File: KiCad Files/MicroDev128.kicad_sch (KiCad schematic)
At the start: 24 parts, among them J1 UPDI Header, J3 GPIO, J4 PWR and ANALOG, SW1 SW_SP3T, SW2 RST, U1 AVR128DB32x-xRXB, U2 LT8653SEV_PBF

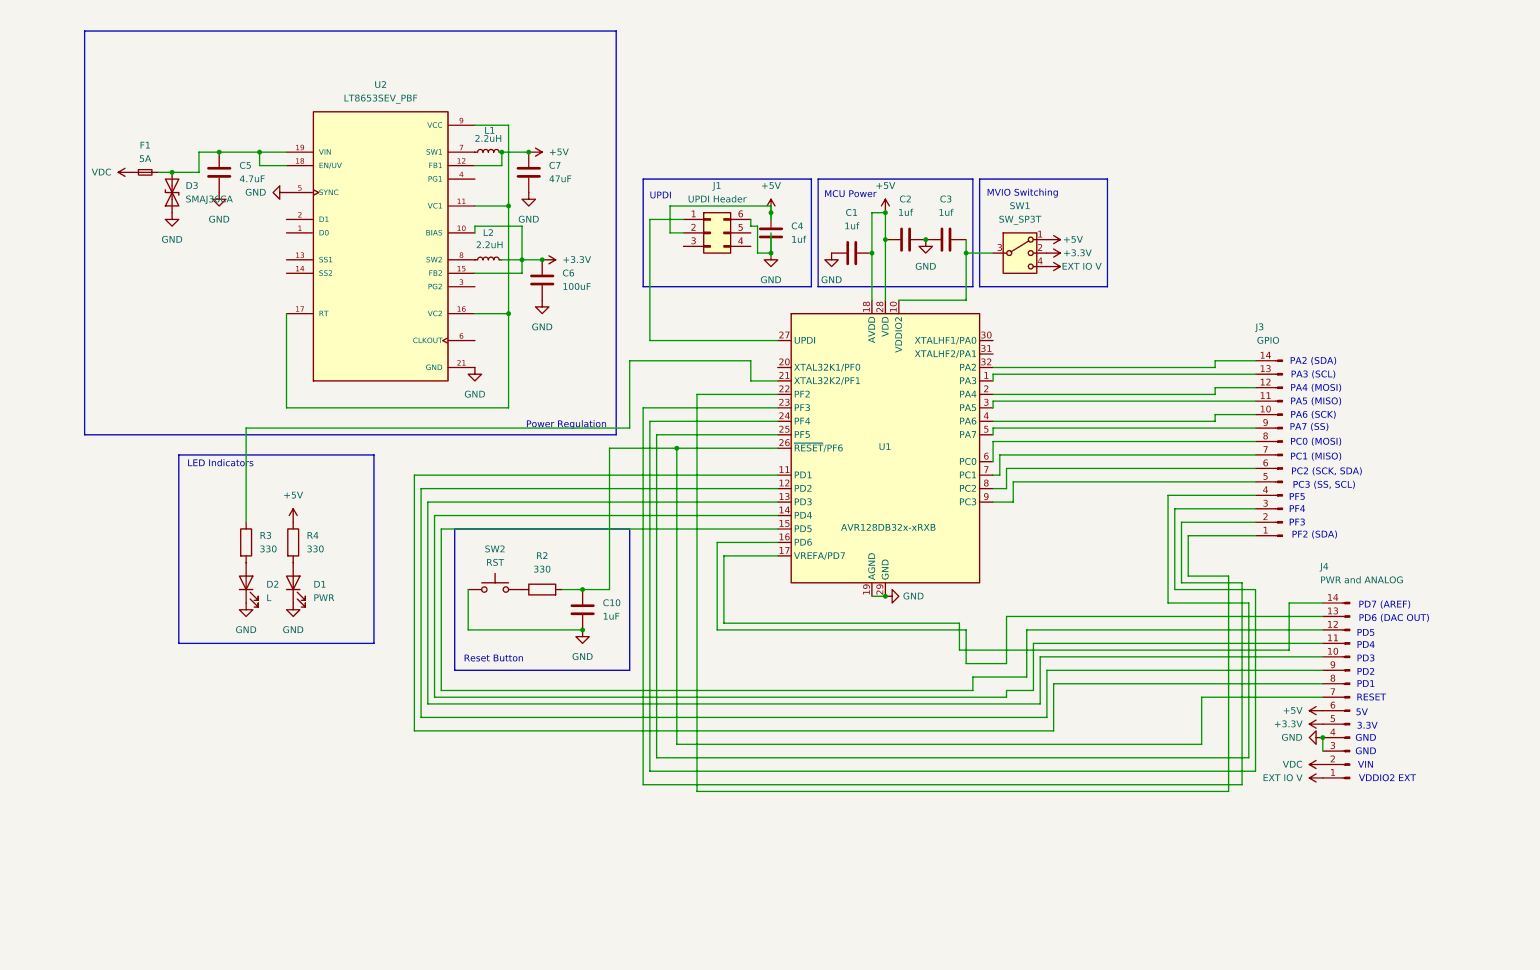
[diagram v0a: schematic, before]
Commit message: Updated PCB, fixed errors, and added more docs
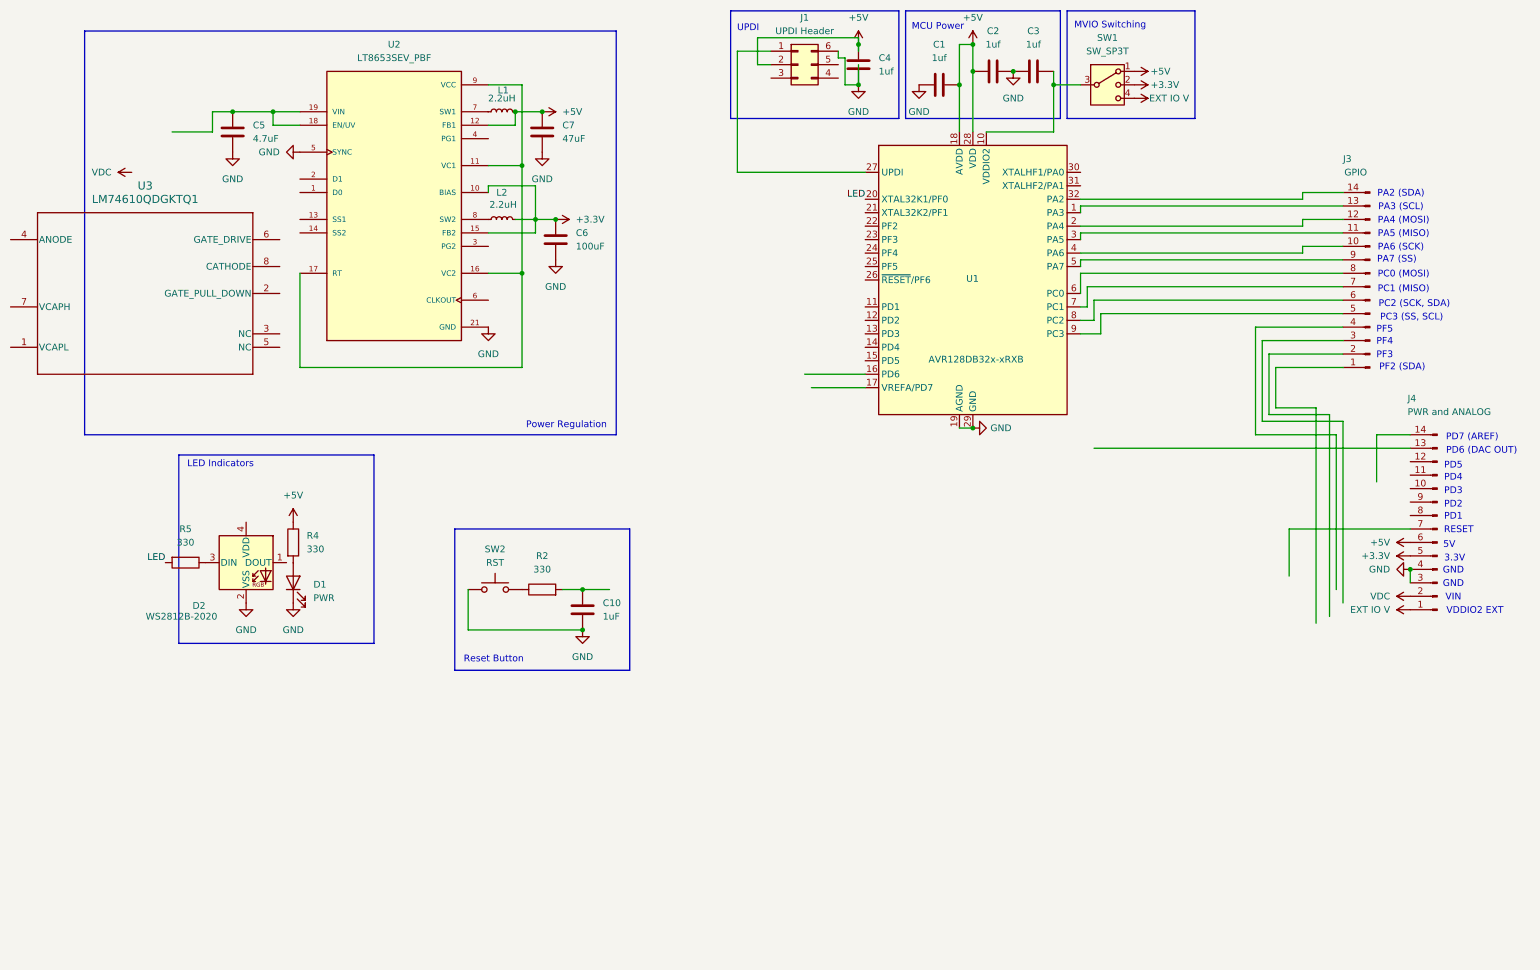
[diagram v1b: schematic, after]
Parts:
- removed D2: L, LED_SMD:LED_0603_1608Metric, symbol Device:LED
- removed D3: SMAJ36CA, Diode_SMD:D_SMA, symbol Device:D_TVS
- removed F1: 5A, Fuse:Fuse_0603_1608Metric, symbol Device:Fuse_Small
- removed R3: 330, Resistor_SMD:R_0402_1005Metric, symbol Device:R
- added D2: WS2812B-2020, LED_SMD:LED_WS2812B-2020_PLCC4_2.0x2.0mm, symbol LED:WS2812B-2020
- added R5: 330, Resistor_SMD:R_0402_1005Metric, symbol Device:R
- added U3: LM74610QDGKTQ1, DGK0008A_N, symbol LM7610:LM74610QDGKTQ1
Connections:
- net GND: now also D2.2 (VSS)
- net at U1.11 (PD1): no longer J4.8 (Pin_8)
- net at U1.12 (PD2): no longer J4.9 (Pin_9)
- net at U1.13 (PD3): no longer J4.10 (Pin_10)
- net at U1.14 (PD4): no longer J4.11 (Pin_11)
- net at U1.15 (PD5): no longer J4.12 (Pin_12)
- net at U1.16 (PD6): no longer J4.13 (Pin_13)
- net at U1.17 (VREFA/PD7): no longer J4.14 (Pin_14)
- net LED: now reaches U1.20 (XTAL32K1/PF0)
- net LED: now also R5.2
- net at U1.22 (PF2): no longer J3.1 (Pin_1)
- net at U1.23 (PF3): no longer J3.2 (Pin_2)
- net at U1.24 (PF4): no longer J3.3 (Pin_3)
- net at U1.25 (PF5): no longer J3.4 (Pin_4)
- net at C10.1, R2.2: no longer J4.7 (Pin_7), U1.26 (~{RESET}/PF6)
- new net: D2.3 (DIN), R5.1
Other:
- moved on the sheet: C1, C2, C3, C4, C5, C6, C7, J1, J3, J4, L1, L2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

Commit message: Started on Rev1B
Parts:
- added C8: 2.2uF, Capacitor_SMD:C_0402_1005Metric, symbol Device:C
- added C9: 100nF, symbol Device:C_Small
- added F1: 5A, Fuse:Fuse_0603_1608Metric, symbol Device:Fuse
- added J2: USB Connector, symbol Connector:USB_C_Receptacle_USB2.0_14P
- added Q1: DMN6040FDE, Package_DFN_QFN:DFN-6-1EP_2x2mm_P0.65mm_EP1.01x1.7mm, symbol Transistor_FET:2N7000
- added U4: CH330N, Package_SO:SOIC-8_3.9x4.9mm_P1.27mm, symbol Interface_USB:CH330N
- C1, C2, C3, C4: footprint Capacitor_SMD:C_0603_1608Metric -> Capacitor_SMD:C_0402_1005Metric
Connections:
- net +5V: now also D2.4 (VDD), U4.5 (VCC); no longer C4.1
- net GND: now also C9.1, U4.3 (GND); no longer J1.6 (Pin_6)
- net VDC: now also F1.1
- net at J1.1 (Pin_1): no longer U1.27 (UPDI)
- net at U1.1 (PA3): no longer J3.13 (Pin_13)
- net at U1.2 (PA4): no longer J3.12 (Pin_12)
- net RST: now reaches U1.26 (~{RESET}/PF6)
- net RST: now also C10.1, R2.2
- net at U1.3 (PA5): no longer J3.11 (Pin_11)
- net at U1.32 (PA2): no longer J3.14 (Pin_14)
- net at U1.4 (PA6): no longer J3.10 (Pin_10)
- net at U1.5 (PA7): no longer J3.9 (Pin_9)
- net at U1.6 (PC0): no longer J3.8 (Pin_8)
- net at U1.7 (PC1): no longer J3.7 (Pin_7)
- net at U1.8 (PC2): no longer J3.6 (Pin_6)
- net at U1.9 (PC3): no longer J3.5 (Pin_5)
- net at C5.1, U2.18 (EN/UV), U2.19 (VIN)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: now also U3.8 (CATHODE), Q1.1 (S)
- net at U3.1 (VCAPL): now also C8.2
- net at U3.2 (GATE_PULL_DOWN): now also U3.6 (GATE_DRIVE), Q1.2 (G)
- net at U3.4 (ANODE): now also F1.2, Q1.3 (D)
- net at U3.7 (VCAPH): now also C8.1
- net EXT IO V: no longer names the net of J4.1 (Pin_1)
- net EXT IO V: no longer SW1.4
- new net: C9.2, U4.8 (V3)
- new net: J2.A1 (GND), J2.A12 (GND), J2.B1 (GND), J2.B12 (GND)
- new net: J2.A4 (VBUS), J2.A9 (VBUS), J2.B4 (VBUS), J2.B9 (VBUS)
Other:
- title: MicroDev128 -> MicroDev128-32P
- moved on the sheet: C10, C4, C5, C6, C7, D1, D2, J3, L1, L2, R2, R4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

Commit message: Updated Naming, and started in dev work
On rev 1B
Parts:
- removed C4: 1uf, Capacitor_SMD:C_0402_1005Metric, symbol Device:C
- removed J1: UPDI Header, Connector_PinHeader_2.54mm:PinHeader_2x03_P2.54mm_Vertical, symbol Connector_Generic:Conn_02x03_Counter_Clockwise
- removed J3: GPIO, Connector_PinHeader_2.54mm:PinHeader_1x14_P2.54mm_Vertical, symbol Connector:Conn_01x14_Pin
- removed J4: PWR and ANALOG, Connector_PinHeader_2.54mm:PinHeader_1x14_P2.54mm_Vertical, symbol Connector:Conn_01x14_Pin
- removed SW1: SW_SP3T, Button_Switch_SMD:SW_SP3T_PCM13, symbol Switch:SW_SP3T
- added 5.1K1: R, Resistor_SMD:R_0402_1005Metric, symbol Device:R
- added D3: D, Diode_SMD:D_SOD-323, symbol Device:D
- added J1: Header 2, Connector_PinHeader_2.54mm:PinHeader_1x15_P2.54mm_Vertical, symbol Connector:Conn_01x15_Pin
- added J3: Header 1, Connector_PinHeader_2.54mm:PinHeader_1x15_P2.54mm_Vertical, symbol Connector:Conn_01x15_Pin
- added R1: 5.1K, Resistor_SMD:R_0402_1005Metric, symbol Device:R
- added R3: 4.7K, Resistor_SMD:R_0402_1005Metric, symbol Device:R
- added U5: 74HC4051, Package_DFN_QFN:DHVQFN-16-1EP_2.5x3.5mm_P0.5mm_EP1x2mm, symbol 74xx:74HC4051
- added U6: TLV70018_SOT353, Package_TO_SOT_SMD:SOT-353_SC-70-5, symbol Regulator_Linear:TLV70018_SOT353
- C3: value 1uf -> 1uF
- C9: footprint (none) -> Capacitor_SMD:C_0402_1005Metric
- J2: footprint (none) -> Connector_USB:USB_C_Receptacle_HRO_TYPE-C-31-M-12
- U3: footprint DGK0008A_N -> Package_SO:VSSOP-8_3x3mm_P0.65mm
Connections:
- net +3.3V: now also J3.6 (Pin_6), U5.15 (A2), U6.1 (IN), U6.3 (EN)
- net +5V: now also D3.1 (K), J3.7 (Pin_7), U5.14 (A1), U5.16 (VCC)
- net GND: now also C3.2, J2.A1 (GND), J2.A12 (GND), J2.B1 (GND), J2.B12 (GND), J2.SH (SHIELD), 5.1K1.2, J3.3 (Pin_3), J3.4 (Pin_4), R1.2, U5.1 (A4), U5.6 (~{E}), U5.7 (VEE), U5.8 (GND), U6.2 (GND); no longer C3.1, U2.5 (SYNC)
- net RST: now also J3.8 (Pin_8)
- net at U4.1 (UD+): now also J2.A6 (D+), J2.B6 (D+)
- net at U4.2 (UD-): now also J2.A7 (D-), J2.B7 (D-)
- net at U4.6 (TXD): now also R3.1
- net UPDI: now reaches U4.7 (RXD)
- net UPDI: now also U1.27 (UPDI), R3.2
- net at U1.1 (PA3): now also J1.12 (Pin_12)
- net VDDIO2: now reaches U1.10 (VDDIO2)
- net VDDIO2: now also U5.3 (A); no longer C3.2
- net at U1.11 (PD1): now also J3.9 (Pin_9)
- net at U1.12 (PD2): now also J3.10 (Pin_10)
- net at U1.13 (PD3): now also J3.11 (Pin_11)
- net at U1.14 (PD4): now also J3.12 (Pin_12)
- net at U1.15 (PD5): now also J3.13 (Pin_13)
- net at U1.16 (PD6): now also J3.14 (Pin_14)
- net at U1.17 (VREFA/PD7): now also J3.15 (Pin_15)
- net at U1.2 (PA4): now also J1.11 (Pin_11)
- net S0: now reaches U1.21 (XTAL32K2/PF1)
- net S0: now also U5.11 (S0)
- net S1: now reaches U1.22 (PF2)
- net S1: now also U5.10 (S1)
- net S2: now reaches U1.23 (PF3)
- net S2: now also U5.9 (S2)
- net PF4: now reaches U1.24 (PF4)
- net PF4: now also J1.2 (Pin_2)
- net PF5: now reaches U1.25 (PF5)
- net PF5: now also J1.3 (Pin_3)
- net at U1.3 (PA5): now also J1.10 (Pin_10)
- net at U1.30 (XTALHF1/PA0): now also J1.15 (Pin_15)
- net at U1.31 (XTALHF2/PA1): now also J1.14 (Pin_14)
- net at U1.32 (PA2): now also J1.13 (Pin_13)
- net at U1.4 (PA6): now also J1.9 (Pin_9)
- net at U1.5 (PA7): now also J1.8 (Pin_8)
- net at U1.6 (PC0): now also J1.7 (Pin_7)
- net at U1.7 (PC1): now also J1.6 (Pin_6)
- net at U1.8 (PC2): now also J1.5 (Pin_5)
- net at U1.9 (PC3): now also J1.4 (Pin_4)
- net at U2.11 (VC1), U2.16 (VC2), U2.17 (RT)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: now also U2.5 (SYNC)
- net at J2.A4 (VBUS), J2.A9 (VBUS), J2.B4 (VBUS)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: now also D3.2 (A)
- net at J2.A5 (CC1): now also R1.1
- net at J2.B5 (CC2): now also 5.1K1.1
- net VDC renamed PWR
- net PWR: now also J3.2 (Pin_2)
- new net +1V8: C3.1, J3.5 (Pin_5), U5.12 (A3), U6.5 (OUT)
- new net EXT: J3.1 (Pin_1), U5.13 (A0)
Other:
- note added: "1.8V"
- note added: "PA0"
- note added: "PA1"
- note removed: "PF2 (SDA)"
- note removed: "PF3"
- note removed: "UPDI"
- moved on the sheet: C1, C2, U1
